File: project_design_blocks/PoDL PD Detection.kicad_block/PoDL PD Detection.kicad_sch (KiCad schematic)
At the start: 9 parts, among them Q301 DMN62D1LFD-7, U304 TLV7031QDCKRQ1

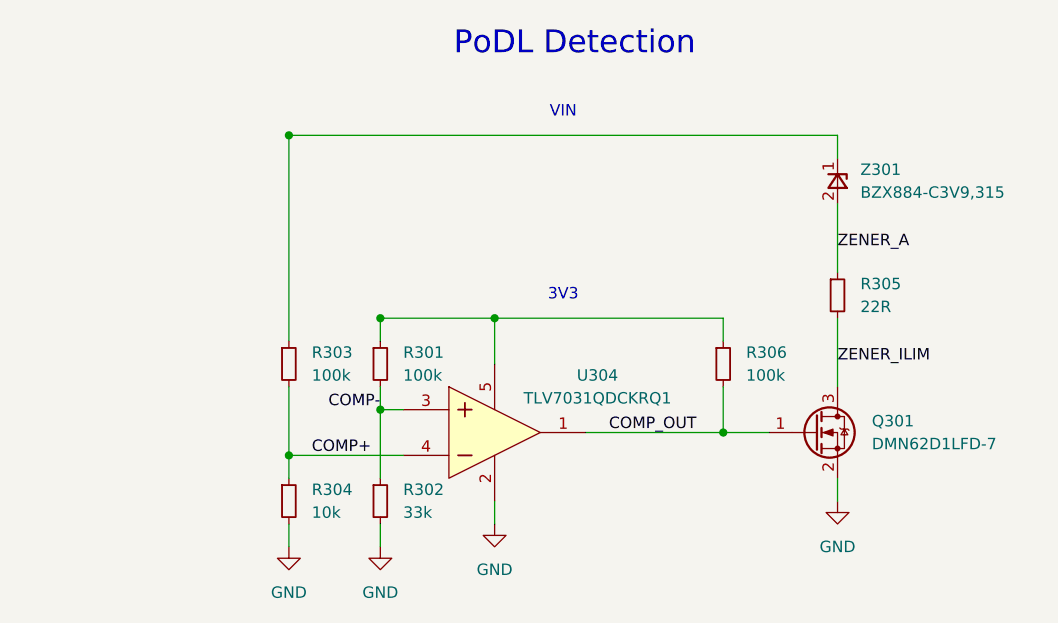
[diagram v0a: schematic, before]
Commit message: Consolidated some libraries
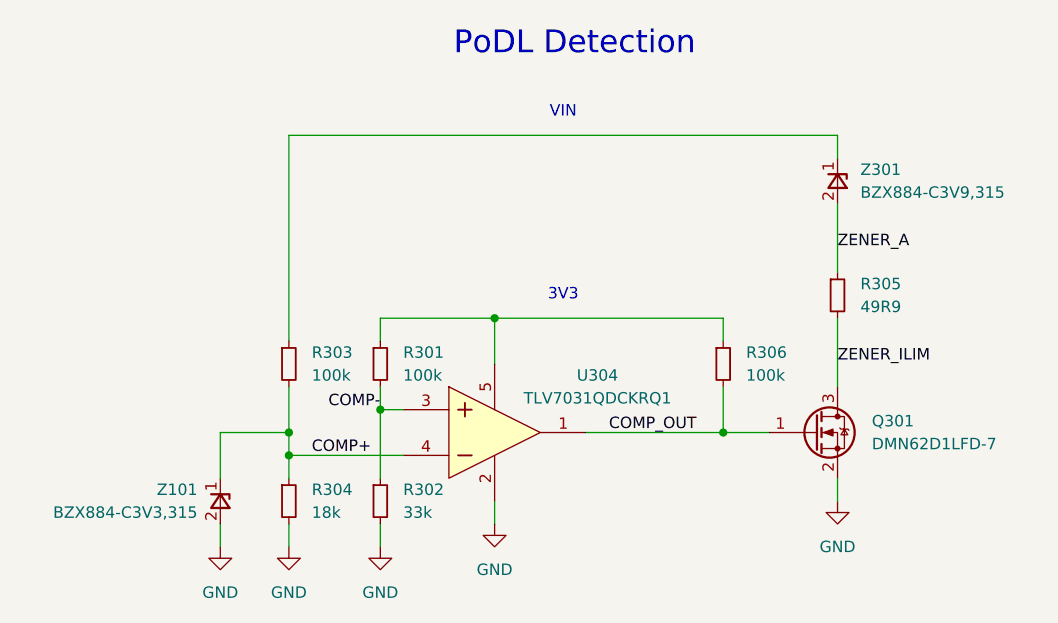
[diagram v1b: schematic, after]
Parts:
- added Z101: BZX884-C3V3,315, project_footprints:BZX884, symbol BZX884:BZX884-C3V3,315
- R304: value 10k -> 18k
- R305: value 22R -> 49R9
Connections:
- net COMP+: now also Z101.1 (K)
- net GND: now also Z101.2 (A)
